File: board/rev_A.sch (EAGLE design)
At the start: 25 parts, among them IC1 STM32F303K8T, IC2 MCP6292, U1 V_REG_LDOSMD, U2 V_REG_LDOSMD

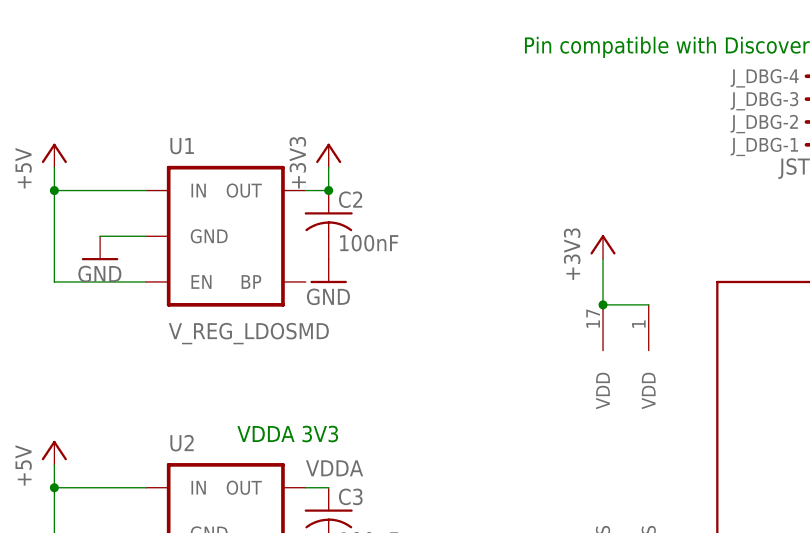
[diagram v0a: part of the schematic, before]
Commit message: [Boards] Adding bypass cap and optimizing routing.
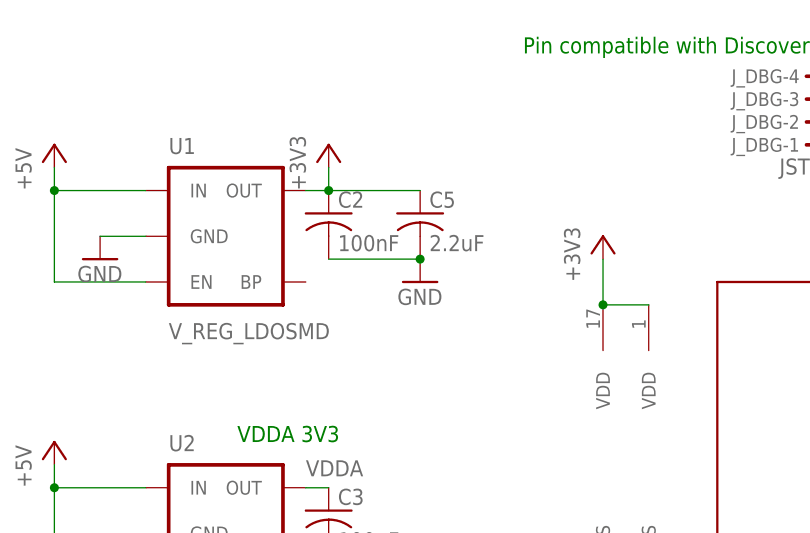
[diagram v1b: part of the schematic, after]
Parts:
- added C5: 2.2uF, resistor:C-USC0603
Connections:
- net +3V3: now also C5.1
- net GND: now also C5.2
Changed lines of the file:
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@@
 <part name="GND5" library="supply1" deviceset="GND" device=""/>
 <part name="C4" library="resistor" deviceset="C-US" device="C0603" value="1uF"/>
+<part name="C5" library="resistor" deviceset="C-US" device="C0603" value="2.2uF"/>
 </parts>
 <sheets>
@@
 <instance part="C3" gate="G$1" x="40.64" y="58.42"/>
 <instance part="GND8" gate="1" x="40.64" y="50.8"/>
-<instance part="GND9" gate="1" x="40.64" y="83.82"/>
+<instance part="GND9" gate="1" x="50.8" y="83.82"/>
 <instance part="R1" gate="G$1" x="201.93" y="87.63" smashed="yes" rot="R90">
 <attribute name="NAME" x="200.4314" y="83.82" size="1.778" layer="95" rot="R90"/>
@@
 <instance part="GND5" gate="1" x="29.21" y="17.78"/>
 <instance part="C4" gate="G$1" x="59.69" y="27.94" rot="MR0"/>
+<instance part="C5" gate="G$1" x="50.8" y="91.44"/>
 </instances>
 <busses>
@@
 <pinref part="C2" gate="G$1" pin="2"/>
 <pinref part="GND9" gate="1" pin="GND"/>
+<pinref part="C5" gate="G$1" pin="2"/>
+<junction x="50.8" y="86.36"/>
+<wire x1="50.8" y1="86.36" x2="40.64" y2="86.36" width="0.1524" layer="91"/>
 </segment>
 <segment>
@@
 <pinref part="C2" gate="G$1" pin="1"/>
 <junction x="40.64" y="93.98"/>
-</segment>
-<segment>
+<pinref part="C5" gate="G$1" pin="1"/>
+<wire x1="50.8" y1="93.98" x2="40.64" y2="93.98" width="0.1524" layer="91"/>
+</segment>
+<segment>

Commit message: [Board] Prepping for panels, cleaning labels, adding optional shunt resistors.
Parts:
- added R11, R12: 5K, resistor:R-EU_0411/12
- C1, C2, C3, C4, C5: device resistor:C-USC0603 -> resistor:C-EUC0603
- R1, R10, R2, R3, R4, R5, R6, R7, R8, R9: device resistor:R-US_R0603 -> resistor:R-EU_R0603
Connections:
- net VR1+: now also R11.1
- net VR1-: now also R11.2
- net VR2+: now also R12.1
- net VR2-: now also R12.2
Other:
- note added: "Shunts"
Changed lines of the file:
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@@
 <part name="P+2" library="supply1" deviceset="+5V" device=""/>
 <part name="GND4" library="supply1" deviceset="GND" device=""/>
-<part name="R4" library="resistor" deviceset="R-US_" device="R0603" value="470K"/>
-<part name="R5" library="resistor" deviceset="R-US_" device="R0603" value="470K"/>
-<part name="C2" library="resistor" deviceset="C-US" device="C0603" value="100nF"/>
-<part name="C3" library="resistor" deviceset="C-US" device="C0603" value="100nF"/>
+<part name="R4" library="resistor" deviceset="R-EU_" device="R0603" value="470K"/>
+<part name="R5" library="resistor" deviceset="R-EU_" device="R0603" value="470K"/>
+<part name="C2" library="resistor" deviceset="C-EU" device="C0603" value="100nF"/>
+<part name="C3" library="resistor" deviceset="C-EU" device="C0603" value="100nF"/>
 <part name="GND8" library="supply1" deviceset="GND" device=""/>
 <part name="GND9" library="supply1" deviceset="GND" device=""/>
-<part name="R1" library="resistor" deviceset="R-US_" device="R0603" value="10K"/>
-<part name="R8" library="resistor" deviceset="R-US_" device="R0603" value="10K"/>
+<part name="R1" library="resistor" deviceset="R-EU_" device="R0603" value="10K"/>
+<part name="R8" library="resistor" deviceset="R-EU_" device="R0603" value="10K"/>
 <part name="D1" library="diode" deviceset="DIODE-2AC|CA" device="SOT23" value="BAV170"/>
 <part name="IC2" library="linear" deviceset="MCP602" device="SN" value="MCP6292"/>
-<part name="R2" library="resistor" deviceset="R-US_" device="R0603" value="470K"/>
-<part name="R3" library="resistor" deviceset="R-US_" device="R0603" value="470K"/>
-<part name="R6" library="resistor" deviceset="R-US_" device="R0603" value="10K"/>
-<part name="R7" library="resistor" deviceset="R-US_" device="R0603" value="10K"/>
+<part name="R2" library="resistor" deviceset="R-EU_" device="R0603" value="470K"/>
+<part name="R3" library="resistor" deviceset="R-EU_" device="R0603" value="470K"/>
+<part name="R6" library="resistor" deviceset="R-EU_" device="R0603" value="10K"/>
+<part name="R7" library="resistor" deviceset="R-EU_" device="R0603" value="10K"/>
 <part name="D2" library="diode" deviceset="DIODE-2AC|CA" device="SOT23" value="BAV170"/>
 <part name="J1" library="SparkFun-Connectors" deviceset="CONN_04" device="LOCK"/>
@@
 <part name="P+3" library="supply1" deviceset="+5V" device=""/>
 <part name="D3" library="SparkFun-LED" deviceset="LED-GREEN" device="0603" value="GREEN"/>
-<part name="R9" library="resistor" deviceset="R-US_" device="R0603" value="1K"/>
+<part name="R9" library="resistor" deviceset="R-EU_" device="R0603" value="1K"/>
 <part name="P+4" library="supply1" deviceset="+5V" device=""/>
 <part name="GND6" library="supply1" deviceset="GND" device=""/>
 <part name="J_SER" library="con-jst" deviceset="?4B-ZR" device="B" value="JST-ZH"/>
 <part name="J_DBG" library="con-jst" deviceset="?4B-ZR" device="B" value="JST-ZH"/>
-<part name="R10" library="resistor" deviceset="R-US_" device="R0603" value="10K"/>
+<part name="R10" library="resistor" deviceset="R-EU_" device="R0603" value="10K"/>
 <part name="GND7" library="supply1" deviceset="GND" device=""/>
-<part name="C1" library="resistor" deviceset="C-US" device="C0603" value="100nF"/>
+<part name="C1" library="resistor" deviceset="C-EU" device="C0603" value="100nF"/>
 <part name="GND5" library="supply1" deviceset="GND" device=""/>
-<part name="C4" library="resistor" deviceset="C-US" device="C0603" value="1uF"/>
-<part name="C5" library="resistor" deviceset="C-US" device="C0603" value="2.2uF"/>
+<part name="C4" library="resistor" deviceset="C-EU" device="C0603" value="1uF"/>
+<part name="C5" library="resistor" deviceset="C-EU" device="C0603" value="2.2uF"/>
+<part name="R11" library="resistor" deviceset="R-EU_" device="0411/12" value="5K"/>
+<part name="R12" library="resistor" deviceset="R-EU_" device="0411/12" value="5K"/>
 </parts>
 <sheets>
@@
 <text x="20.32" y="7.62" size="1.778" layer="91">Open Drain, 3.3V tolerant</text>
 <text x="62.23" y="109.22" size="1.778" layer="91">Pin compatible with Discovery board debug port</text>
+<text x="100.33" y="-3.81" size="1.778" layer="91">Shunts</text>
 </plain>
 <instances>
@@
 <instance part="C4" gate="G$1" x="59.69" y="27.94" rot="MR0"/>
 <instance part="C5" gate="G$1" x="50.8" y="91.44"/>
+<instance part="R11" gate="G$1" x="105.41" y="11.43"/>
+<instance part="R12" gate="G$1" x="105.41" y="3.81"/>
 </instances>
 <busses>
@@
 <label x="20.32" y="26.67" size="1.778" layer="95"/>
 </segment>
+<segment>
+<pinref part="R11" gate="G$1" pin="1"/>
+<wire x1="100.33" y1="11.43" x2="88.9" y2="11.43" width="0.1524" layer="91"/>
+<label x="100.33" y="11.43" size="1.778" layer="95" rot="R180"/>
+</segment>
 </net>
 <net name="VR1-" class="0">
@@
 <wire x1="20.32" y1="29.21" x2="29.21" y2="29.21" width="0.1524" layer="91"/>
 <label x="20.32" y="29.21" size="1.778" layer="95"/>
+</segment>
+<segment>
+<pinref part="R11" gate="G$1" pin="2"/>
+<wire x1="110.49" y1="11.43" x2="121.92" y2="11.43" width="0.1524" layer="91"/>
+<label x="110.49" y="11.43" size="1.778" layer="95"/>
 </segment>
 </net>
@@
 <label x="20.32" y="31.75" size="1.778" layer="95"/>
 </segment>
+<segment>
+<pinref part="R12" gate="G$1" pin="1"/>
+<wire x1="100.33" y1="3.81" x2="88.9" y2="3.81" width="0.1524" layer="91"/>
+<label x="100.33" y="3.81" size="1.778" layer="95" rot="R180"/>
+</segment>
 </net>
 <net name="VR2-" class="0">
@@
 <label x="20.32" y="34.29" size="1.778" layer="95"/>
 </segment>
-</net>
+<segment>
+<pinref part="R12" gate="G$1" pin="2"/>
+<wire x1="110.49" y1="3.81" x2="121.92" y2="3.81" width="0.1524" layer="91"/>
+<label x="110.49" y="3.81" size="1.778" layer="95"/>
+</segment>
+</net>
